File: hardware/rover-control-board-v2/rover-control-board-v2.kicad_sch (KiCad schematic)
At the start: 58 parts, among them J10 CAN1, J12 XT120, J3 Contactor, J4 XT90_REG_OUT, J5 XT90_REG_RET, J6 OUT, J7 RET, J8 CAN1, J9 CAN1, Q5 MCACD8D5N06YL-TP, Q6 MCACD8D5N06YL-TP, U17 NMUX1308BQ, U18 NMUX1308BQ, U4 LM74700

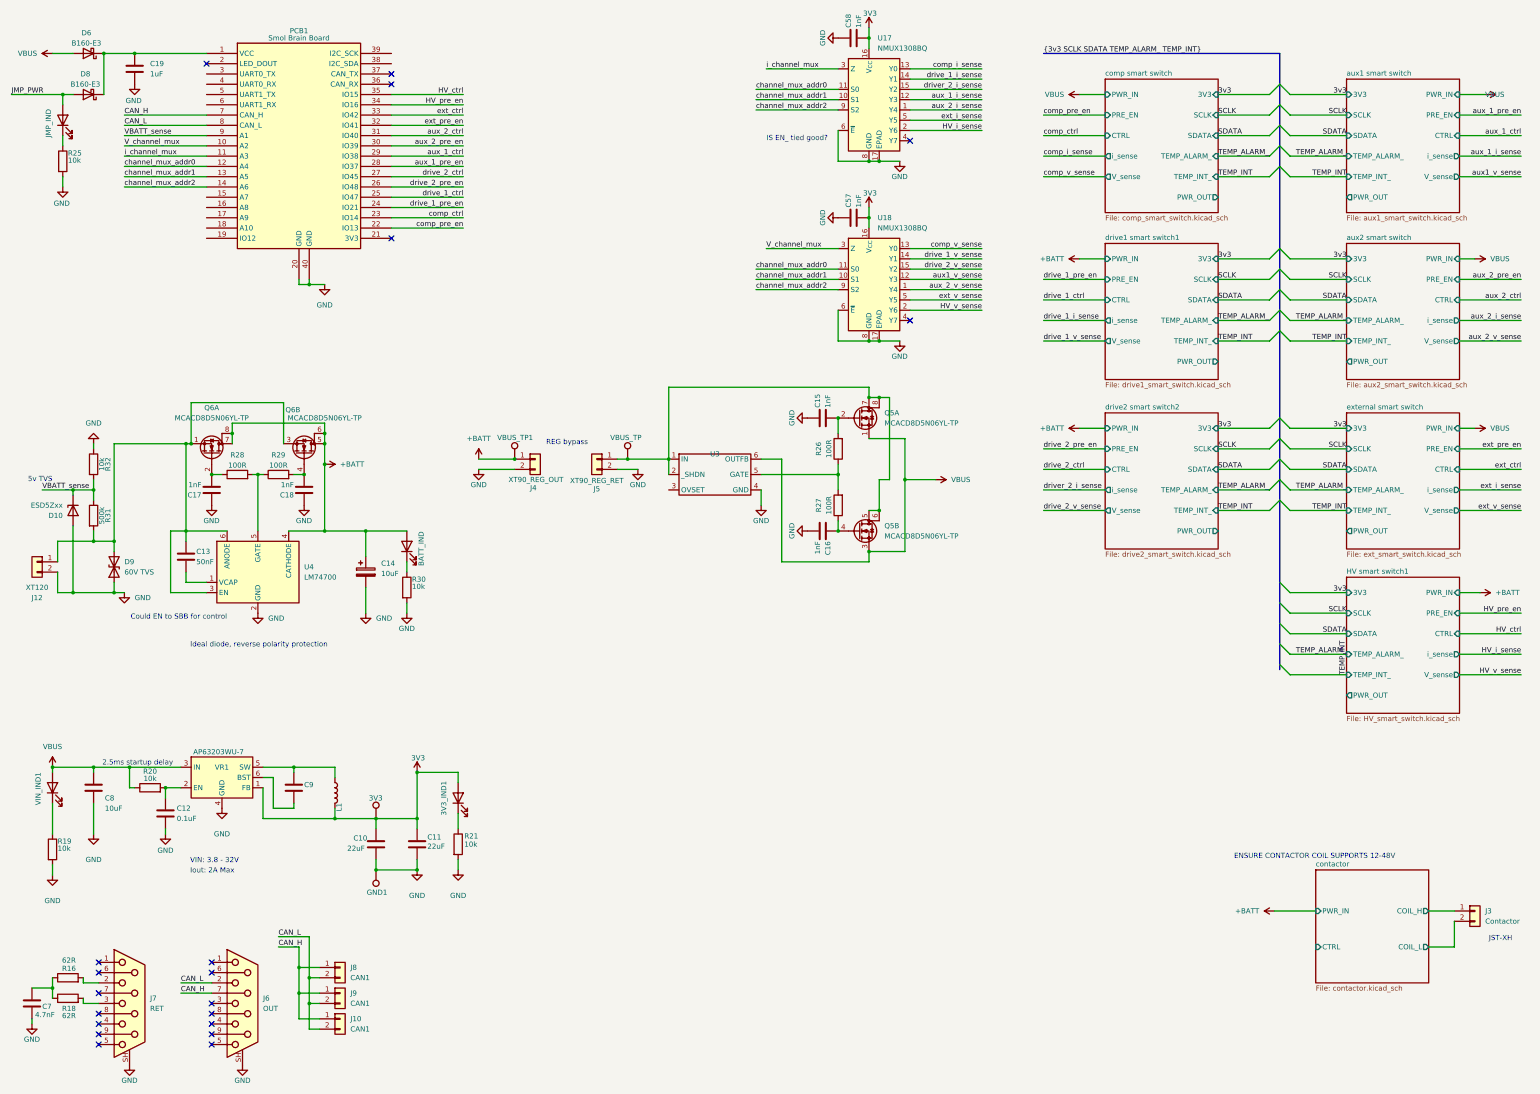
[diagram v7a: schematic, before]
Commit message: Bus routed
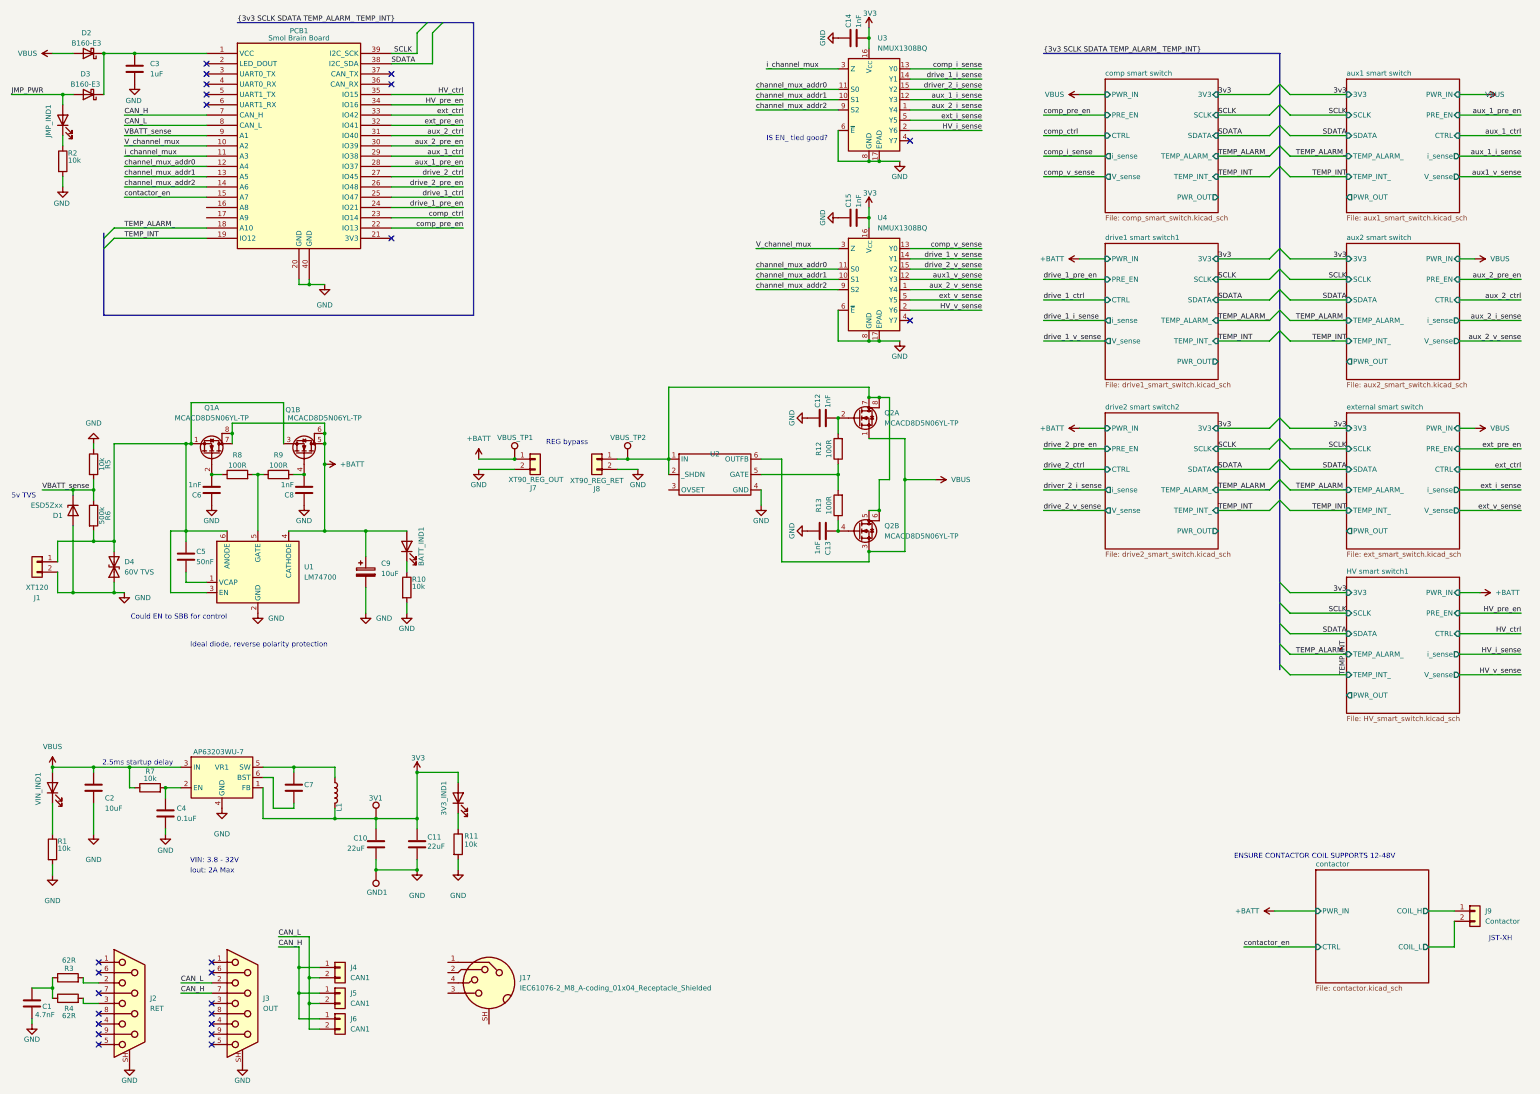
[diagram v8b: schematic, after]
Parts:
- added J17: IEC61076-2_M8_A-coding_01x04_Receptacle_Shielded, symbol Connector:IEC61076-2_M8_A-coding_01x04_Receptacle_Shielded
- renumbered 3V3 to 3V1, BATT_IND to BATT_IND1, C7 to C1, C15 to C12, C16 to C13, C58 to C14, C57 to C15, C8 to C2, C19 to C3, C12 to C4, C13 to C5, C17 to C6, C9 to C7, C18 to C8, C14 to C9, D10 to D1, D6 to D2, D8 to D3, D9 to D4, J12 to J1, J7 to J2, J6 to J3, J8 to J4, J9 to J5, J10 to J6, J4 to J7, J5 to J8, J3 to J9, JMP_IND to JMP_IND1, Q6 to Q1, Q5 to Q2, R19 to R1, R30 to R10, R21 to R11, R26 to R12, R27 to R13, R25 to R2, R16 to R3, R18 to R4, R32 to R5, R31 to R6, R20 to R7, R28 to R8, R29 to R9, U4 to U1, U3 to U2, U17 to U3, U18 to U4, VBUS_TP to VBUS_TP2
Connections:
- net SCLK: now also PCB1.39 (I2C_SCK)
- net SDATA: now also PCB1.38 (I2C_SDA)
- net TEMP_ALARM_: now also PCB1.18 (A10)
- net TEMP_INT: now also PCB1.19 (IO12)
- net contactor_en: now reaches PCB1.15 (A7)
- no-connect marks 20 -> 24
